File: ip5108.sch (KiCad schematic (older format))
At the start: 31 parts, among them IC1 IP5108, IC2 SY8008B, J1 DB9_Female, J2 Conn_01x02, U1 STEPDOWN12_5

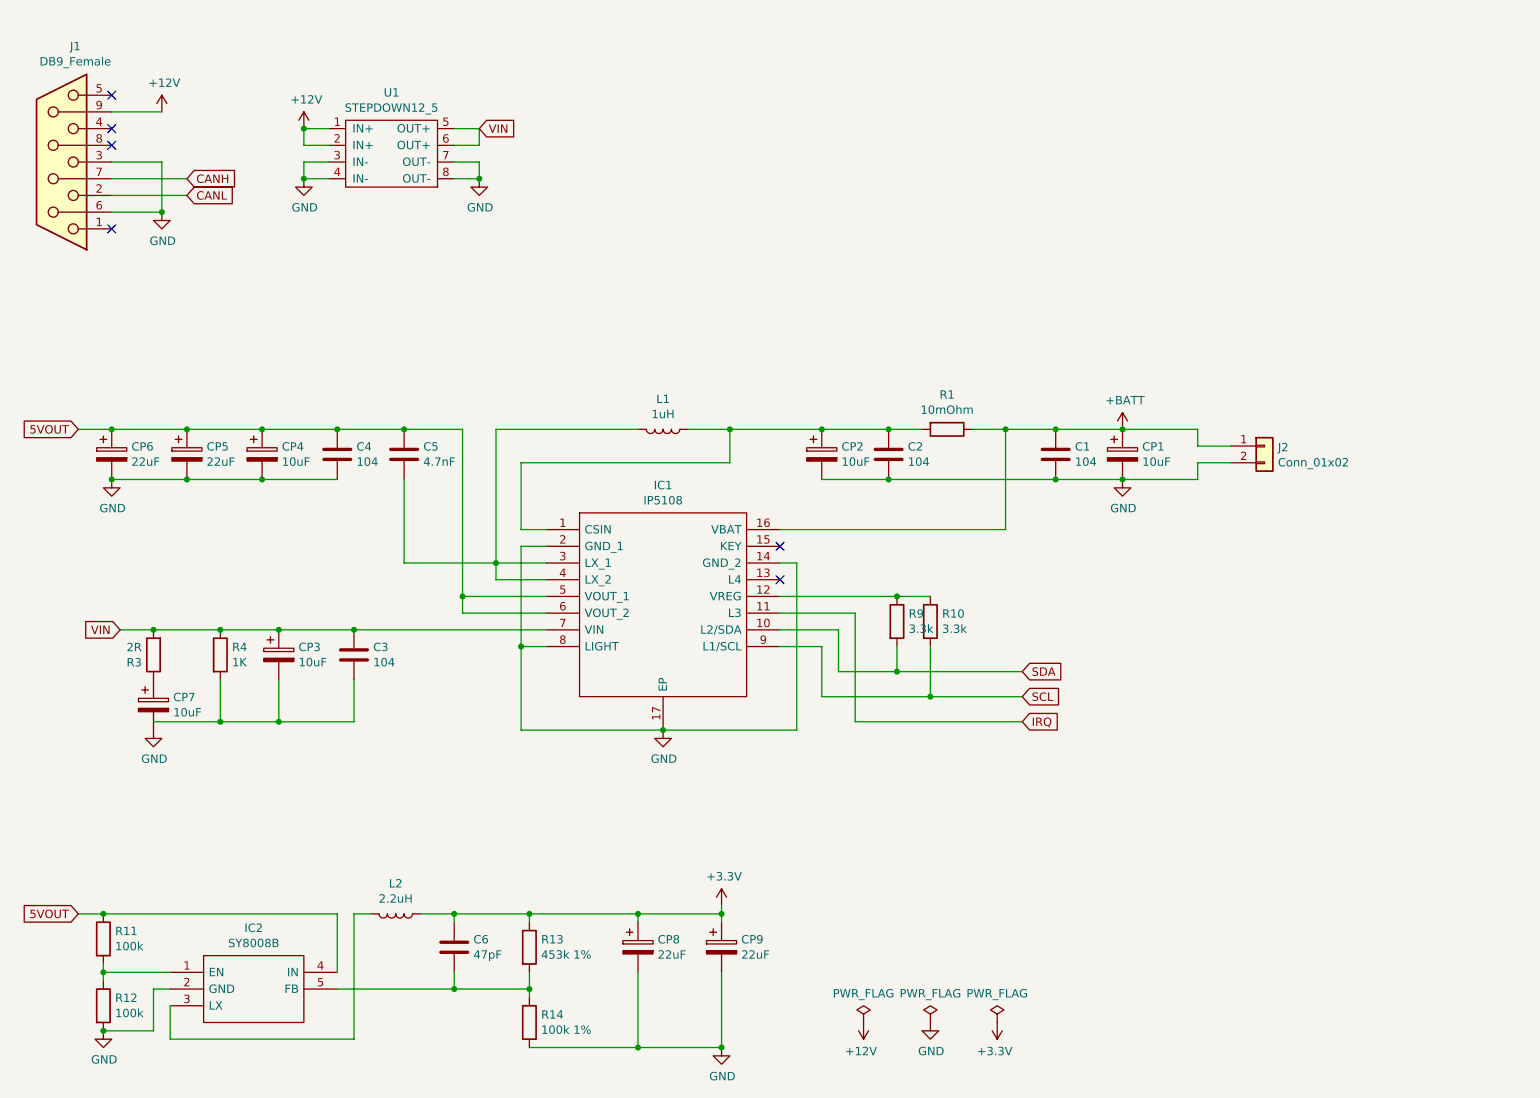
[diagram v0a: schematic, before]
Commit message: IP5108 in Unterschaltplan verschoben
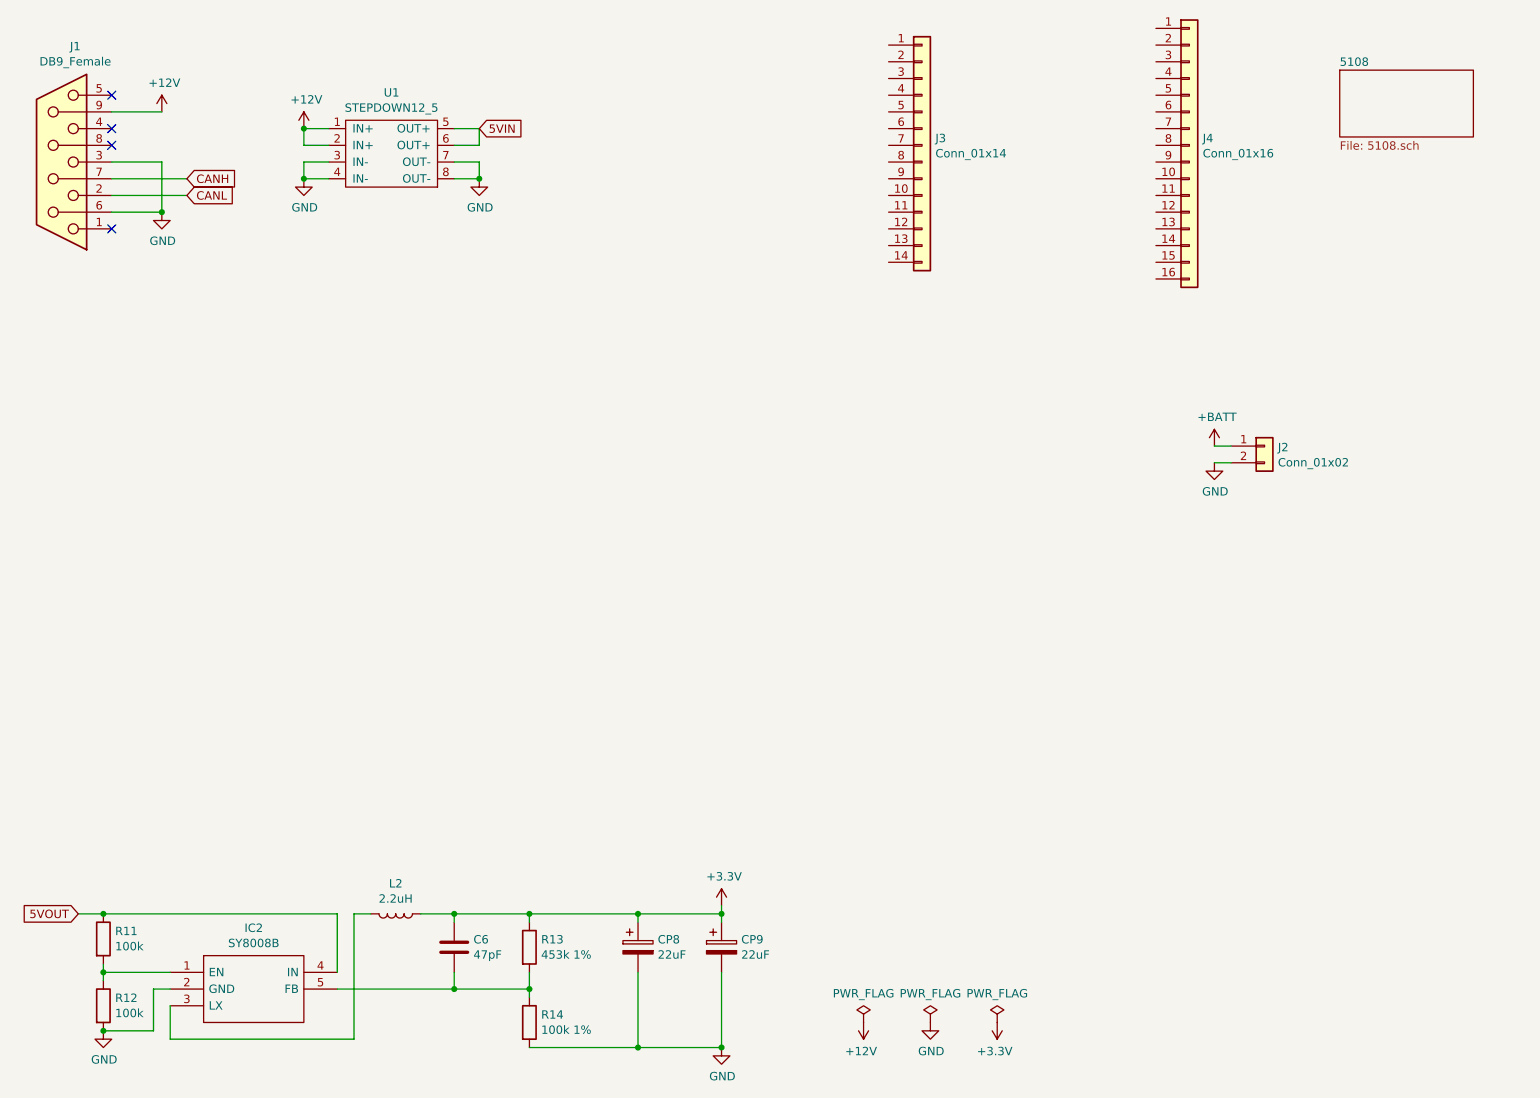
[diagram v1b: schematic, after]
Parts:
- removed C1, C2, C3, C4: 104, Capacitor_SMD:C_0603_1608Metric, symbol Device:C
- removed C5: 4.7nF, Capacitor_SMD:C_0603_1608Metric, symbol Device:C
- removed CP1, CP2, CP3, CP4, CP7: 10uF, Capacitor_Tantalum_SMD:CP_EIA-3528-21_Kemet-B, symbol Device:CP
- removed CP5, CP6: 22uF, Capacitor_Tantalum_SMD:CP_EIA-6032-28_Kemet-C, symbol Device:CP
- removed IC1: IP5108, SamacSys_Parts:SOIC127P600X175-17N, symbol SamacSys_Parts:IP5108
- removed L1: 1uH, SamacSys_Parts:CD54NP470LC, symbol Device:L
- removed R1: 10mOhm, Resistor_SMD:R_1206_3216Metric, symbol Device:R
- removed R10, R9: 3.3k, Resistor_SMD:R_0603_1608Metric, symbol Device:R
- removed R3: 2R, Resistor_SMD:R_0603_1608Metric, symbol Device:R
- removed R4: 1K, Resistor_SMD:R_0603_1608Metric, symbol Device:R
- added J3: Conn_01x14, Connector_PinSocket_2.54mm:PinSocket_1x14_P2.54mm_Vertical, symbol Connector_Generic:Conn_01x14
- added J4: Conn_01x16, Connector_PinSocket_2.54mm:PinSocket_1x16_P2.54mm_Vertical, symbol Connector_Generic:Conn_01x16
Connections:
- net VIN renamed 5VIN
- no-connect marks 6 -> 4

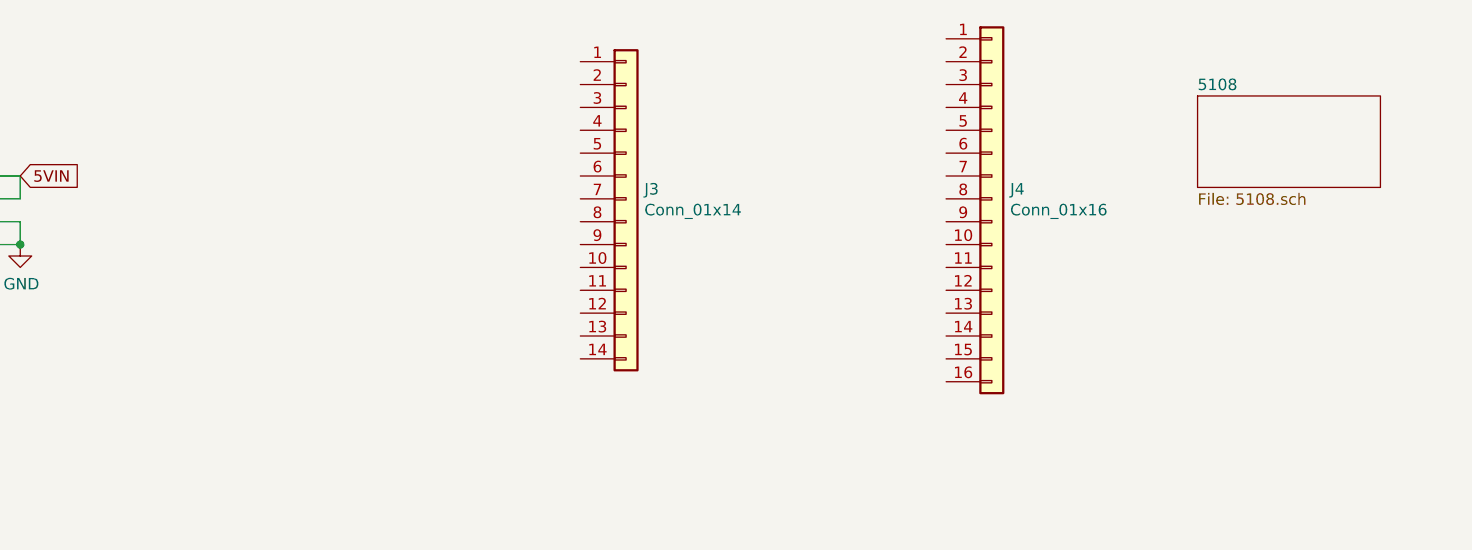
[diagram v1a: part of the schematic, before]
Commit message: IP5108 in Unterverzeichnis verschoben
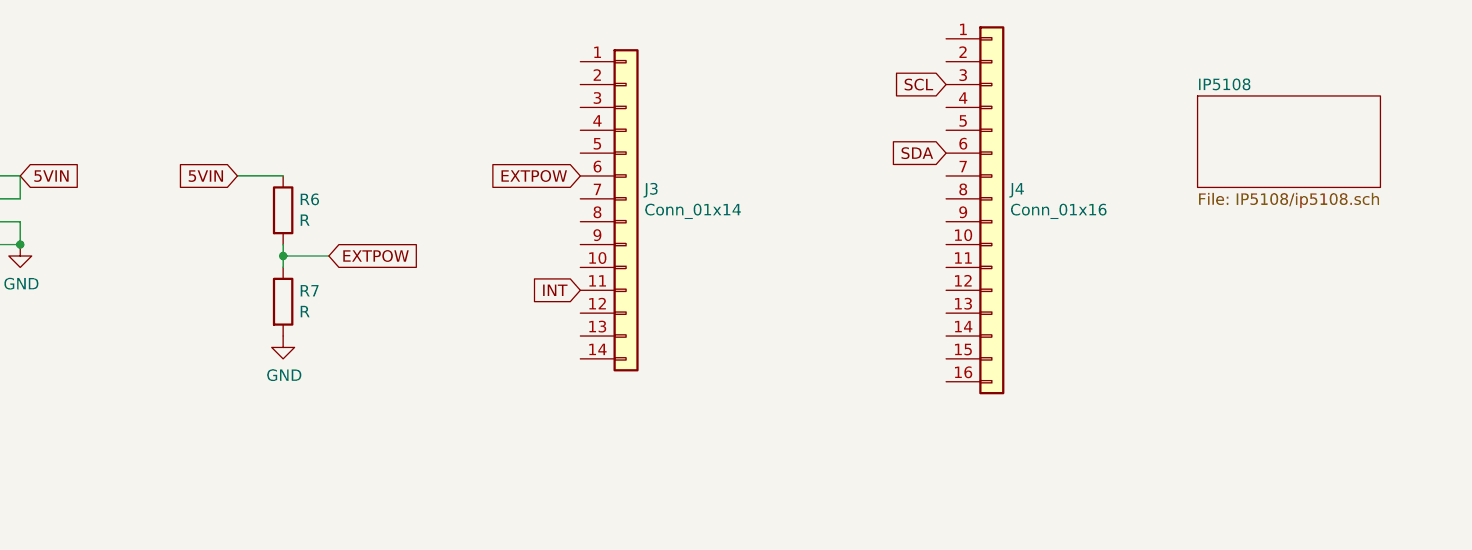
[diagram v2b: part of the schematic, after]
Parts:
- added R6, R7: R, Resistor_SMD:R_0603_1608Metric, symbol Device:R
- L2: footprint SamacSys_Parts:CD54NP470LC -> IP5108:CD54_Inductor
- U1: footprint ip5108:StepDownBreakout -> StepDownBreakout:StepDownBreakout
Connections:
- net 5VIN: now also R6.1
- net GND: now also R7.2
- net INT: now reaches J3.11 (Pin_11)
- net EXTPOW: now reaches J3.6 (Pin_6)
- net EXTPOW: now also R6.2, R7.1
- net SCL: now reaches J4.3 (Pin_3)
- net SDA: now reaches J4.6 (Pin_6)
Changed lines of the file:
@@
 	1250 1950 1700 1950
-$Comp
-L stepdown12_5:STEPDOWN12_5 U1
-U 1 1 60DA3A30
-P 2900 1950
-F 0 "U1" H 2875 1335 50  0000 C CNN
-F 1 "STEPDOWN12_5" H 2875 1426 50  0000 C CNN
-F 2 "ip5108:StepDownBreakout" H 2900 1950 50  0001 C CNN
-F 3 "" H 2900 1950 50  0001 C CNN
-	1    2900 1950
-	-1   0    0    1
-$EndComp
 $Comp
 L power:+12V #PWR0108
@@
 F 0 "L2" V 2769 6250 50  0000 C CNN
 F 1 "2.2uH" V 2860 6250 50  0000 C CNN
-F 2 "SamacSys_Parts:CD54NP470LC" H 2950 6250 50  0001 C CNN
+F 2 "IP5108:CD54_Inductor" H 2950 6250 50  0001 C CNN
 F 3 "~" H 2950 6250 50  0001 C CNN
 	1    2950 6250
@@
 S 8600 1200 800  400
 U 60F1A96E
-F0 "5108" 50
-F1 "5108.sch" 50
+F0 "IP5108" 50
+F1 "IP5108/ip5108.sch" 50
 $EndSheet
 $Comp
@@
 Wire Wire Line
 	7850 3550 7950 3550
+$Comp
+L stepdown12_5:STEPDOWN12_5 U1
+U 1 1 60F48B5B
+P 2900 1950
+F 0 "U1" H 2875 1335 50  0000 C CNN
+F 1 "STEPDOWN12_5" H 2875 1426 50  0000 C CNN
+F 2 "StepDownBreakout:StepDownBreakout" H 2900 1950 50  0001 C CNN
+F 3 "" H 2900 1950 50  0001 C CNN
+	1    2900 1950
+	-1   0    0    1
+$EndComp
+Text GLabel 4400 1550 0    50   Input ~ 0
+5VIN
+$Comp
+L Device:R R6
+U 1 1 60F6141D
+P 4600 1700
+F 0 "R6" H 4670 1746 50  0000 L CNN
+F 1 "R" H 4670 1655 50  0000 L CNN
+F 2 "Resistor_SMD:R_0603_1608Metric" V 4530 1700 50  0001 C CNN
+F 3 "~" H 4600 1700 50  0001 C CNN
+	1    4600 1700
+	1    0    0    -1
+$EndComp
+$Comp
+L Device:R R7
+U 1 1 60F61A44
+P 4600 2100
+F 0 "R7" H 4670 2146 50  0000 L CNN
+F 1 "R" H 4670 2055 50  0000 L CNN
+F 2 "Resistor_SMD:R_0603_1608Metric" V 4530 2100 50  0001 C CNN
+F 3 "~" H 4600 2100 50  0001 C CNN
+	1    4600 2100
+	1    0    0    -1
+$EndComp
+Text GLabel 4800 1900 2    50   Input ~ 0
+EXTPOW
+Wire Wire Line
+	4400 1550 4600 1550
+Wire Wire Line
+	4600 1850 4600 1900
+Wire Wire Line
+	4600 1900 4800 1900
+Connection ~ 4600 1900
+Wire Wire Line
+	4600 1900 4600 1950
+$Comp
+L power:GND #PWR0120
+U 1 1 60F64C82
+P 4600 2250
+F 0 "#PWR0120" H 4600 2000 50  0001 C CNN
+F 1 "GND" H 4605 2077 50  0000 C CNN
+F 2 "" H 4600 2250 50  0001 C CNN
+F 3 "" H 4600 2250 50  0001 C CNN
+	1    4600 2250
+	1    0    0    -1
+$EndComp
+Text GLabel 5900 1550 0    50   Input ~ 0
+EXTPOW
+Text GLabel 7500 1450 0    50   Input ~ 0
+SDA
+Text GLabel 7500 1150 0    50   Input ~ 0
+SCL
+Text GLabel 5900 2050 0    50   Input ~ 0
+INT
 $EndSCHEMATC
